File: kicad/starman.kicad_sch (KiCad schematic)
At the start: 229 parts, among them J1 M20-8771246, J10 PJ-063AH, J11 Conn_02x01, J2 M20-8771246, J3 M20-8771246, J4 ESW-106-44-T-S, J5 PH2-06-UA, J6 ESW-112-44-T-S, J7 Conn_01x10, J8 ESW-112-44-T-S, J9 Conn_01x10, SW1 PTS810 SJM 250 SMTR LFS, SW2 PTS810 SJM 250 SMTR LFS, U1 ESP32-S2-MINI-1, U10 LED1642GWTTR, U11 AZ1084CS2-ADJ, U12 BA33BC0FP-E2, U2 LED1642GWTTR, U3 LED1642GWTTR, U4 LED1642GWTTR, U5 LED1642GWTTR, U6 LED1642GWTTR, U7 LED1642GWTTR, U8 LED1642GWTTR, U9 LED1642GWTTR, X1 ECS-2333-300, X2 ECS-2333-300, X3 ECS-2333-300

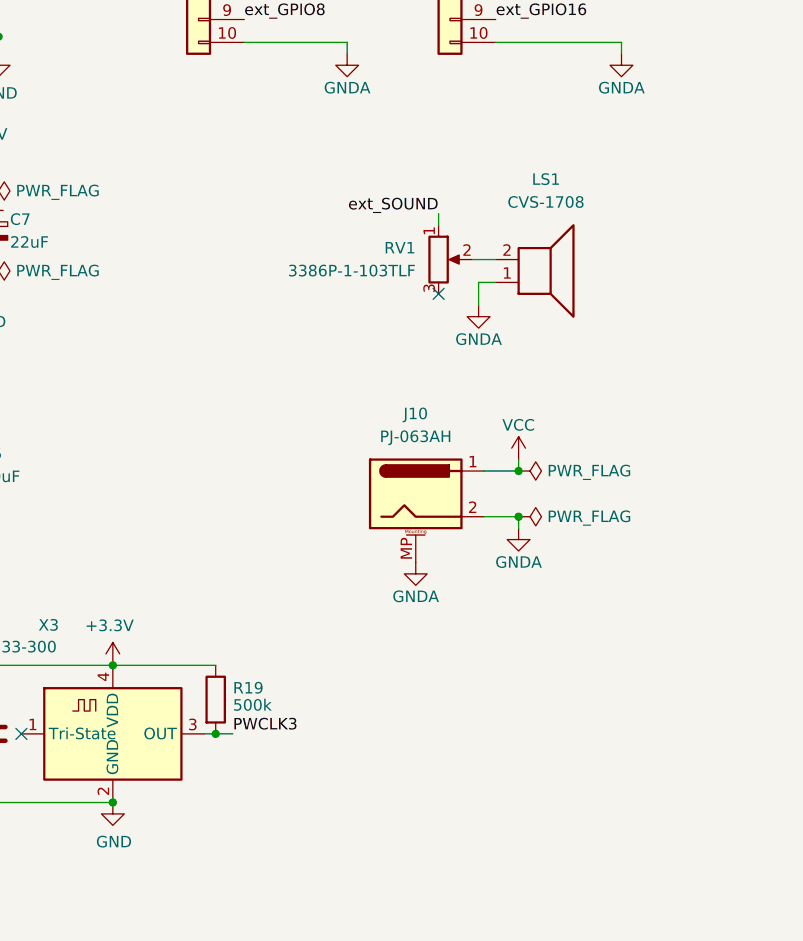
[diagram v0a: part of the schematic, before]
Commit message: Added an LM386 amplifier to ext module
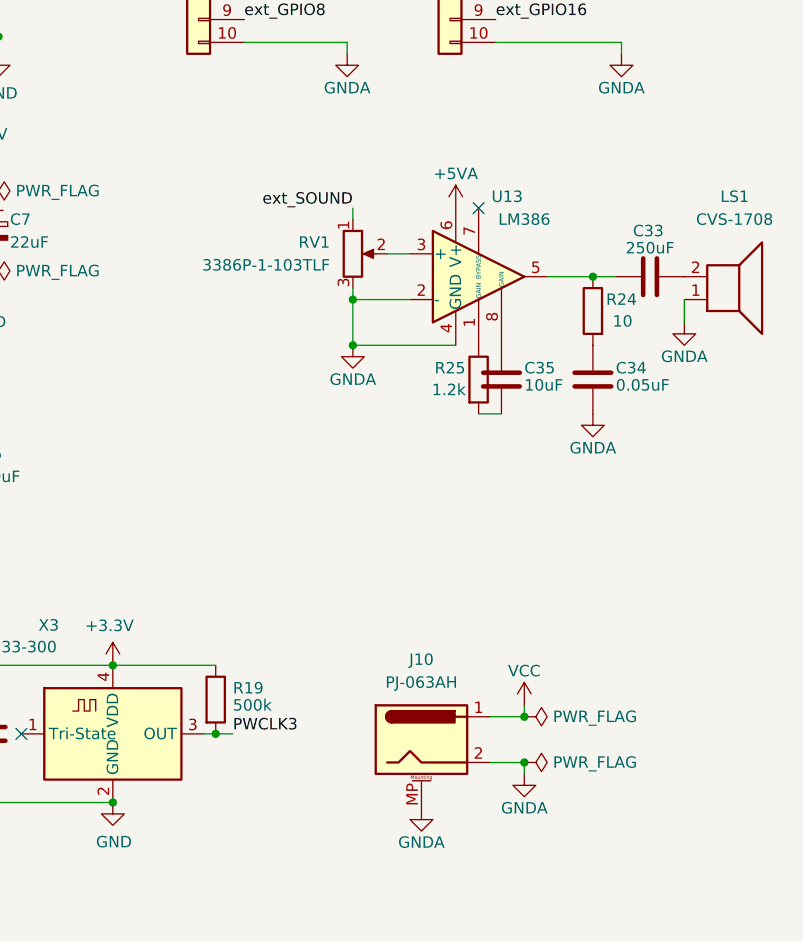
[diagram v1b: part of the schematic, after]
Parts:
- added C33: 250uF, Capacitor_SMD:C_0805_2012Metric, symbol Device:C
- added C34: 0.05uF, Capacitor_SMD:C_0805_2012Metric, symbol Device:C
- added C35: 10uF, Capacitor_SMD:C_0805_2012Metric, symbol Device:C
- added R24: 10, Resistor_SMD:R_0805_2012Metric, symbol Device:R
- added R25: 1.2k, Resistor_SMD:R_0805_2012Metric, symbol Device:R
- added U13: LM386, Package_SO:VSSOP-8_3.0x3.0mm_P0.65mm, symbol Amplifier_Audio:LM386
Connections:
- net +5VA: now also U13.6 (V+)
- net GNDA: now also RV1.3, C34.2, U13.2 (-), U13.4 (GND)
- net at LS1.2: now also C33.1; no longer RV1.2
- new net: RV1.2, U13.3 (+)
- new net: C33.2, R24.1, U13.5
- new net: R25.1, U13.1 (GAIN)
- new net: C35.1, U13.8 (GAIN)
- new net: C35.2, R25.2
- new net: C34.1, R24.2
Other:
- moved on the sheet: J10, LS1, RV1

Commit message: Replace LM386 with IS31AP4991
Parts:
- removed U13: LM386, Package_SO:VSSOP-8_3.0x3.0mm_P0.65mm, symbol Amplifier_Audio:LM386
- added U13: IS31AP4991-SLS2, Package_SO:MSOP-8_3x3mm_P0.65mm, symbol Amplifier_Audio:IS31AP4991-SLS2
- C33: value 250uF -> 100nF
- C34: value 0.05uF -> 1uF
- C35: value 10uF -> 0.47uF
- R24: value 10 -> 20k
- R25: value 1.2k -> 20k
- RV1: value 3386P-1-103TLF -> 20k
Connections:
- net +5VA: now also C34.1, R24.1, U13.6 (V+)
- net GNDA: now also C35.2, U13.7 (GND); no longer LS1.1, RV1.3
- net ext_SOUND: now also C33.2; no longer RV1.1
- net MUTE: now reaches U1.25 (GPIO21)
- net MUTE: now also J1.4 (Pin_4)
- net ext_MUTE: now reaches J6.4 (Pin_4)
- net ext_MUTE: now also R24.2, U13.1 (~{SDB})
- net at LS1.2: now also U13.8; no longer C33.1
- net at RV1.2: now also LS1.1, U13.5
- net at R25.1: now also RV1.1, U13.4 (-)
- net at C35.1: now also U13.2 (BYP), U13.3 (+)
- net at R25.2: now also C33.1; no longer C35.2
- no-connect marks 21 -> 18
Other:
- moved on the sheet: LS1, R25, RV1

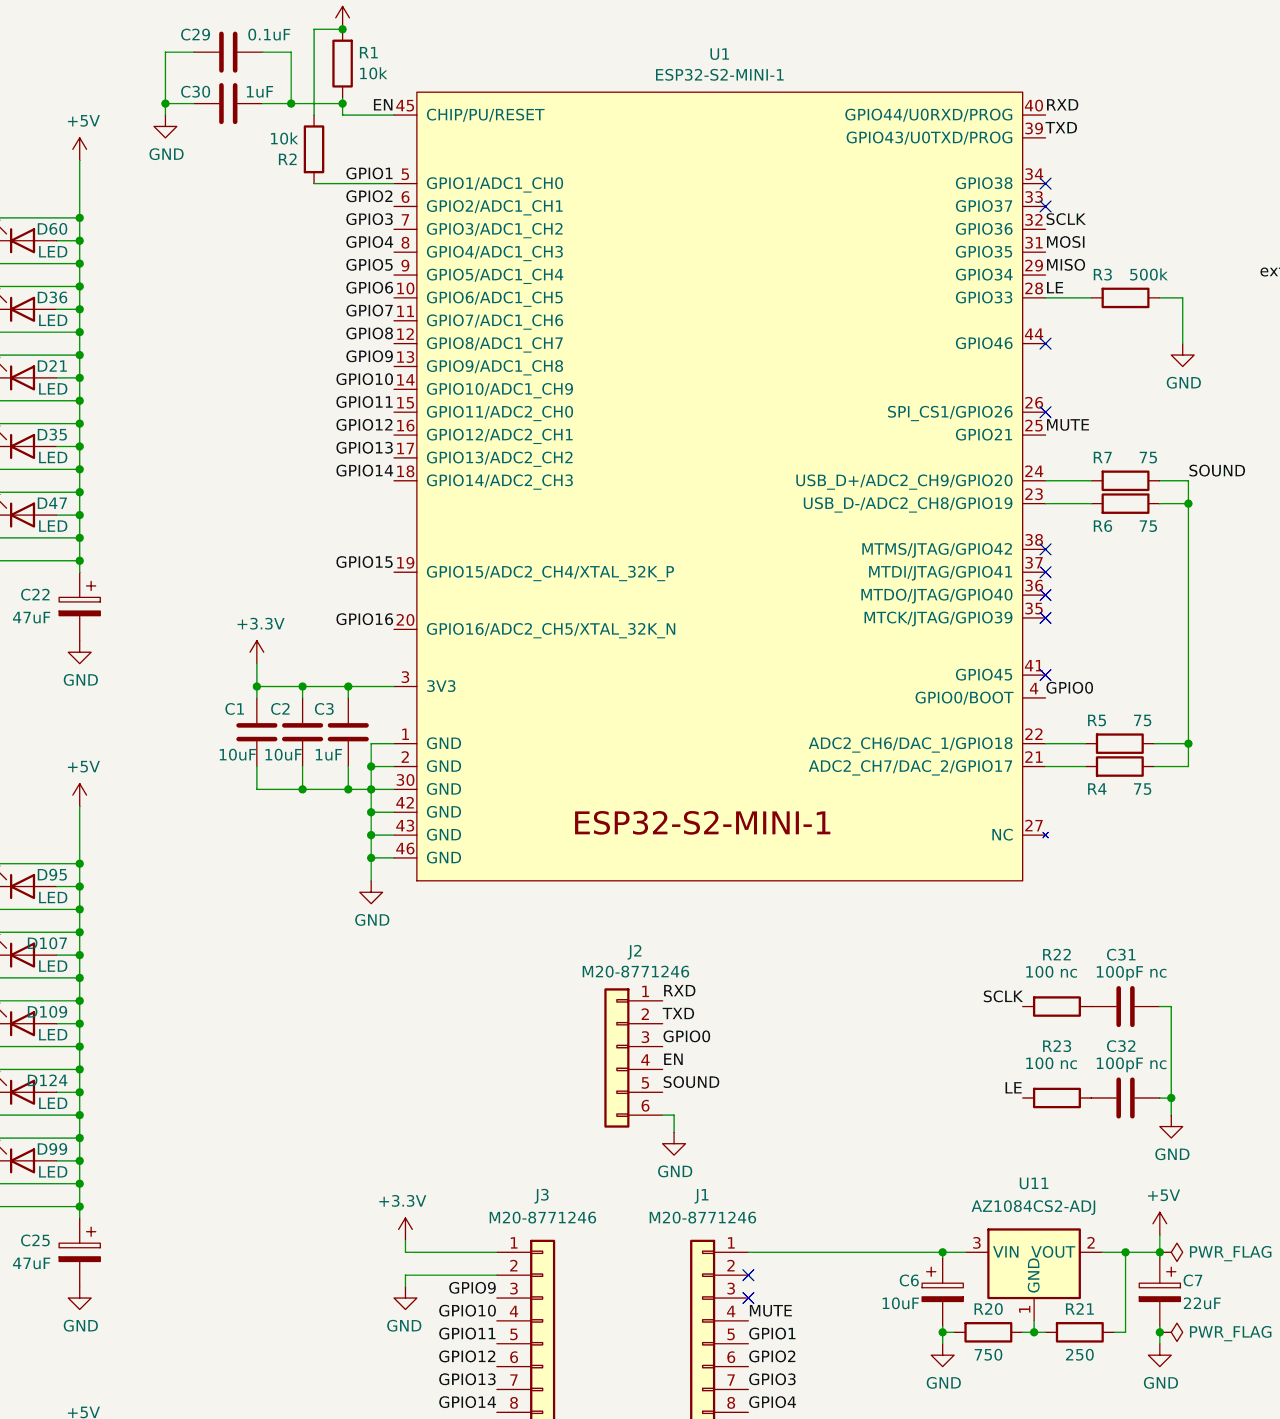
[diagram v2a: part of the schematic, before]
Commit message: Add on a power switch and status light
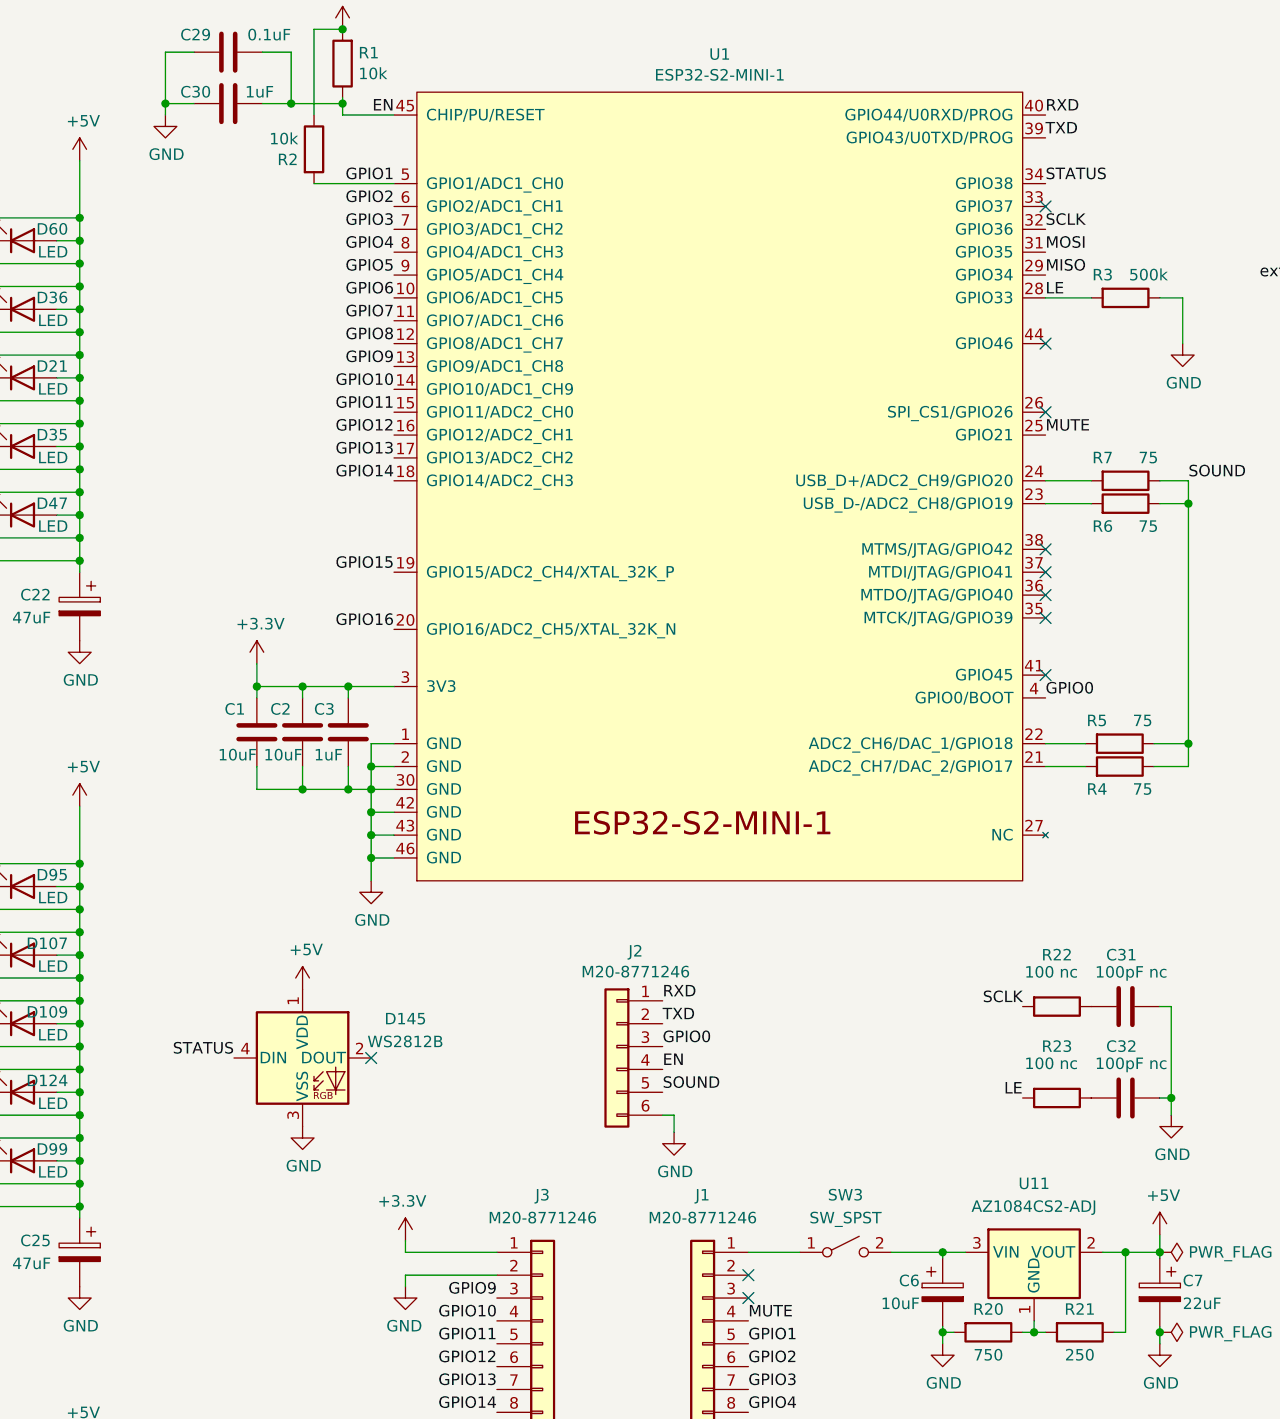
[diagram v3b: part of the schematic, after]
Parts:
- added D145: WS2812B, LED_SMD:LED_WS2812B_PLCC4_5.0x5.0mm_P3.2mm, symbol LED:WS2812B
- added SW3: SW_SPST, Button_Switch_SMD:SW_DIP_SPSTx01_Slide_9.78x4.72mm_W8.61mm_P2.54mm, symbol Switch:SW_SPST
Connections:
- net +5V: now also D145.1 (VDD)
- net GND: now also D145.3 (VSS)
- net STATUS: now reaches U1.34 (GPIO38)
- net STATUS: now also D145.4 (DIN)
- net at C6.1, U11.3 (VIN): now also SW3.2 (B); no longer J1.1 (Pin_1)
- new net: J1.1 (Pin_1), SW3.1 (A)
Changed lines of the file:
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@@
   (junction (at 238.76 29.845) (diameter 0) (color 0 0 0 0)
   )
-  (junction (at 311.15 157.48) (diameter 0) (color 0 0 0 0)
-  )
   (junction (at 215.265 224.155) (diameter 0) (color 0 0 0 0)
   )
@@
   (junction (at 144.145 139.7) (diameter 0) (color 0 0 0 0)
   )
+  (junction (at 311.15 157.48) (diameter 0) (color 0 0 0 0)
+  )
   (junction (at 73.025 191.135) (diameter 0) (color 0 0 0 0)
   )
@@
   (no_connect (at 322.58 93.345))
   (no_connect (at 322.58 56.515))
-  (no_connect (at 322.58 64.135))
   (no_connect (at 289.56 160.02))
   (no_connect (at 289.56 162.56))
@@
   (no_connect (at 322.58 81.915))
   (no_connect (at 363.855 80.01))
+  (no_connect (at 247.65 135.89))
   (no_connect (at 322.58 41.275))
   (no_connect (at 364.49 30.48))
@@
   (no_connect (at 322.58 86.995))
   (no_connect (at 398.145 187.325))
+  (no_connect (at 322.58 64.135))
   (no_connect (at 238.125 217.805))
   (no_connect (at 339.09 217.805))
-  (no_connect (at 322.58 38.735))
   (wire (pts (xy 116.205 139.7) (xy 126.365 139.7))
     (stroke (width 0) (type default) (color 0 0 0 0))
@@
     (stroke (width 0) (type default) (color 0 0 0 0))
   )
+  (wire (pts (xy 289.56 157.48) (xy 295.275 157.48))
+    (stroke (width 0) (type default) (color 0 0 0 0))
+  )
   (wire (pts (xy 144.145 142.24) (xy 141.605 142.24))
     (stroke (width 0) (type default) (color 0 0 0 0))
@@
     (stroke (width 0) (type default) (color 0 0 0 0))
   )
-  (wire (pts (xy 289.56 157.48) (xy 311.15 157.48))
-    (stroke (width 0) (type default) (color 0 0 0 0))
-  )
   (wire (pts (xy 215.265 121.92) (xy 215.265 124.46))
     (stroke (width 0) (type default) (color 0 0 0 0))
@@
     (stroke (width 0) (type default) (color 0 0 0 0))
   )
+  (wire (pts (xy 305.435 157.48) (xy 311.15 157.48))
+    (stroke (width 0) (type default) (color 0 0 0 0))
+  )
   (wire (pts (xy 45.085 47.625) (xy 55.245 47.625))
     (stroke (width 0) (type default) (color 0 0 0 0))
@@
     (effects (font (size 1.27 1.27)) (justify right bottom))
   )
+  (label "STATUS" (at 322.58 38.735 0)
+    (effects (font (size 1.27 1.27)) (justify left bottom))
+  )
   (label "GPIO4" (at 250.19 46.355 180)
     (effects (font (size 1.27 1.27)) (justify right bottom))
@@
     (effects (font (size 1.27 1.27)) (justify left bottom))
   )
+  (label "STATUS" (at 232.41 135.89 180)
+    (effects (font (size 1.27 1.27)) (justify right bottom))
+  )
   (label "SCLK" (at 156.845 52.705 180)
     (effects (font (size 1.27 1.27)) (justify right bottom))
@@
     (pin "6")
   )
+  (symbol (lib_id "Switch:SW_SPST") (at 300.355 157.48 0) (unit 1)
+    (in_bom yes) (on_board yes) (fields_autoplaced)
+    (property "Reference" "SW3" (id 0) (at 300.355 151.13 0))
+    (property "Value" "SW_SPST" (id 1) (at 300.355 153.67 0))
+    (property "Footprint" "Button_Switch_SMD:SW_DIP_SPSTx01_Slide_9.78x4.72mm_W8.61mm_P2.54mm" (id 2) (at 300.355 157.48 0)
+      (effects (font (size 1.27 1.27)) hide)
+    )
+    (property "Datasheet" "~" (id 3) (at 300.355 157.48 0)
+      (effects (font (size 1.27 1.27)) hide)
+    )
+    (pin "1")
+    (pin "2")
+  )
   (symbol (lib_id "power:+5VA") (at 405.765 99.06 0) (unit 1)
     (in_bom yes) (on_board yes)
@@
     (pin "2")
   )
+  (symbol (lib_id "power:GND") (at 240.03 143.51 0) (unit 1)
+    (in_bom yes) (on_board yes)
+    (property "Reference" "#PWR068" (id 0) (at 240.03 149.86 0)
+      (effects (font (size 1.27 1.27)) hide)
+    )
+    (property "Value" "GND" (id 1) (at 240.157 147.9042 0))
+    (property "Footprint" "" (id 2) (at 240.03 143.51 0)
+      (effects (font (size 1.27 1.27)) hide)
+    )
+    (property "Datasheet" "" (id 3) (at 240.03 143.51 0)
+      (effects (font (size 1.27 1.27)) hide)
+    )
+    (pin "1")
+  )
   (symbol (lib_id "Device:C_Polarized") (at 144.145 229.235 0) (mirror y) (unit 1)
     (in_bom yes) (on_board yes)
@@
     (pin "1")
   )
+  (symbol (lib_id "LED:WS2812B") (at 240.03 135.89 0) (unit 1)
+    (in_bom yes) (on_board yes) (fields_autoplaced)
+    (property "Reference" "D145" (id 0) (at 251.46 131.5593 0))
+    (property "Value" "WS2812B" (id 1) (at 251.46 134.0993 0))
+    (property "Footprint" "LED_SMD:LED_WS2812B_PLCC4_5.0x5.0mm_P3.2mm" (id 2) (at 241.3 143.51 0)
+      (effects (font (size 1.27 1.27)) (justify left top) hide)
+    )
+    (property "Datasheet" "https://cdn-shop.adafruit.com/datasheets/WS2812B.pdf" (id 3) (at 242.57 145.415 0)
+      (effects (font (size 1.27 1.27)) (justify left top) hide)
+    )
+    (pin "1")
+    (pin "2")
+    (pin "3")
+    (pin "4")
+  )
   (symbol (lib_id "Connector_Generic:Conn_01x12") (at 358.775 87.63 0) (mirror y) (unit 1)
     (in_bom yes) (on_board yes)
@@
     (pin "2")
   )
+  (symbol (lib_id "power:+5V") (at 240.03 128.27 0) (unit 1)
+    (in_bom yes) (on_board yes)
+    (property "Reference" "#PWR067" (id 0) (at 240.03 132.08 0)
+      (effects (font (size 1.27 1.27)) hide)
+    )
+    (property "Value" "+5V" (id 1) (at 240.411 123.8758 0))
+    (property "Footprint" "" (id 2) (at 240.03 128.27 0)
+      (effects (font (size 1.27 1.27)) hide)
+    )
+    (property "Datasheet" "" (id 3) (at 240.03 128.27 0)
+      (effects (font (size 1.27 1.27)) hide)
+    )
+    (pin "1")
+  )
   (symbol (lib_id "power:GNDA") (at 405.765 78.74 0) (unit 1)
     (in_bom yes) (on_board yes)
@@
       (reference "#PWR066") (unit 1) (value "+3.3V") (footprint "")
     )
+    (path "/81efba4f-2cd0-4979-bfdc-7a3eabe2901e"
+      (reference "#PWR067") (unit 1) (value "+5V") (footprint "")
+    )
+    (path "/38537501-7dc9-47ee-8290-3af809424a45"
+      (reference "#PWR068") (unit 1) (value "GND") (footprint "")
+    )
     (path "/d45aee87-203e-43ff-b11a-2cad667b5b60"
       (reference "#PWR069") (unit 1) (value "GND") (footprint "")
@@
       (reference "D144") (unit 1) (value "LED") (footprint "starman:LED_Osram_Lx_P47F_D2mm_ReverseMount")
     )
+    (path "/42a33d65-5ec1-4cc3-ba31-451358aab287"
+      (reference "D145") (unit 1) (value "WS2812B") (footprint "LED_SMD:LED_WS2812B_PLCC4_5.0x5.0mm_P3.2mm")
+    )
     (path "/00000000-0000-0000-0000-00006736c4ff"
       (reference "J1") (unit 1) (value "M20-8771246") (footprint "Connector_PinHeader_2.54mm:PinHeader_1x12_P2.54mm_Vertical_SMD_Pin1Right")
@@
       (reference "SW2") (unit 1) (value "PTS810 SJM 250 SMTR LFS") (footprint "Button_Switch_SMD:SW_SPST_PTS810")
     )
+    (path "/345e8491-7841-488c-a81c-5c44839b6770"
+      (reference "SW3") (unit 1) (value "SW_SPST") (footprint "Button_Switch_SMD:SW_DIP_SPSTx01_Slide_9.78x4.72mm_W8.61mm_P2.54mm")
+    )
     (path "/00000000-0000-0000-0000-00006255a4d8"
